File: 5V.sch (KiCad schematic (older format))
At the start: 13 parts, among them U2 LMZ13608, U3 LTC2946

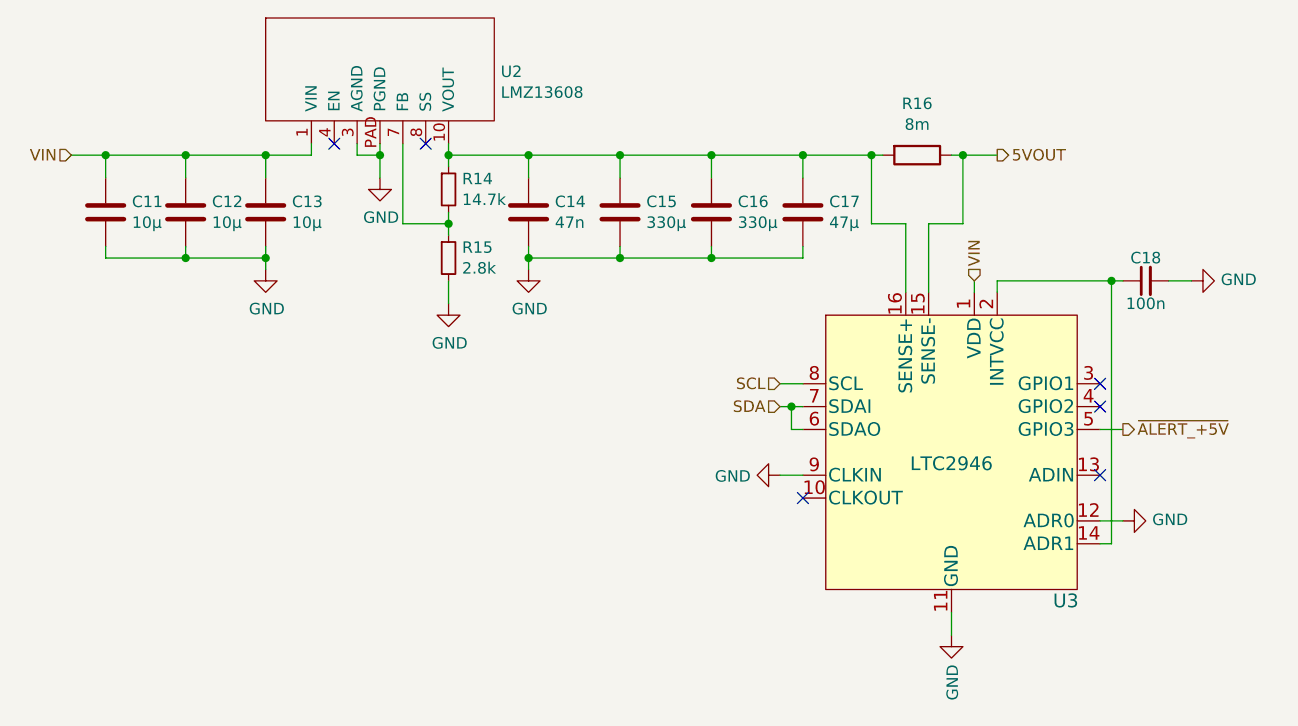
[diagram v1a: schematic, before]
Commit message: LMZM23600 from kicad libs
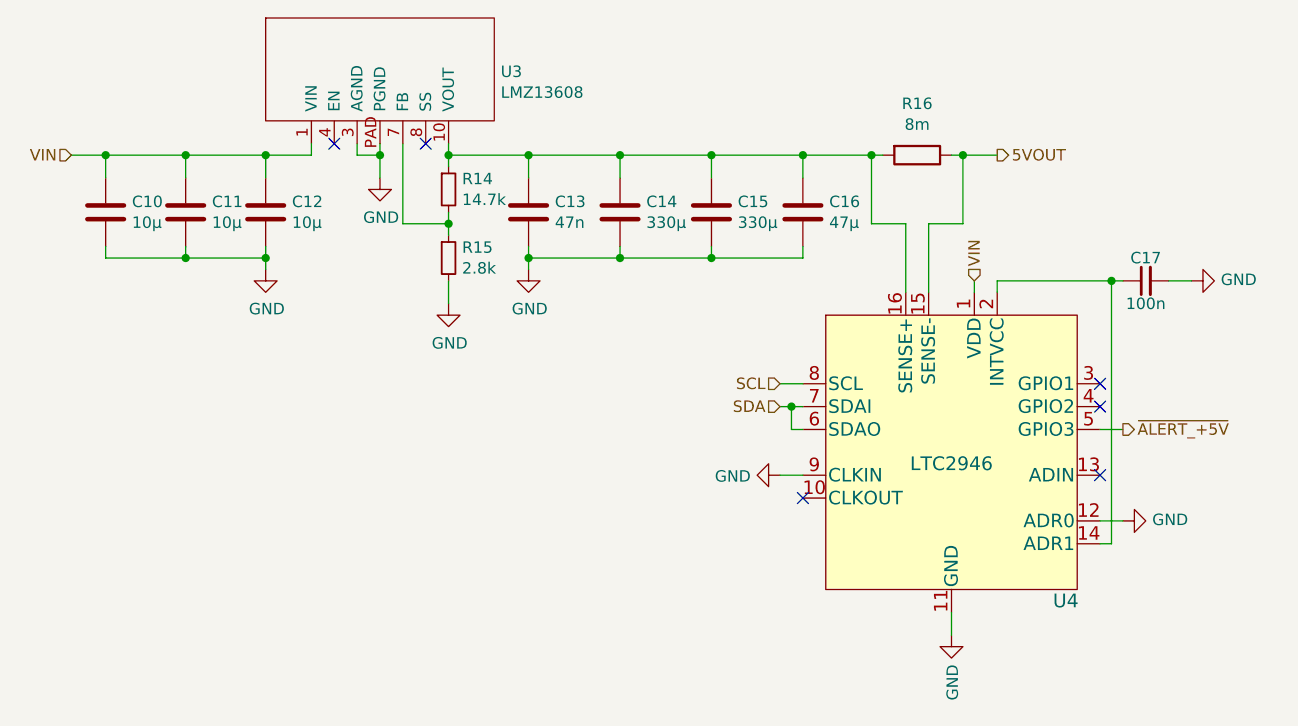
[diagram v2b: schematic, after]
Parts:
- renumbered C11 to C10, C12 to C11, C13 to C12, C14 to C13, C15 to C14, C16 to C15, C17 to C16, C18 to C17, U2 to U3, U3 to U4
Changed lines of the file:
@@
 $EndDescr
 $Comp
-L power:GND #PWR018
+L power:GND #PWR025
 U 1 1 5C2D1347
 P 6550 4350
-F 0 "#PWR018" H 6550 4100 50  0001 C CNN
+F 0 "#PWR025" H 6550 4100 50  0001 C CNN
 F 1 "GND" V 6555 4222 50  0000 R CNN
 F 2 "" H 6550 4350 50  0001 C CNN
@@
 $EndComp
 $Comp
-L Device:C_Small C18
+L Device:C_Small C17
 U 1 1 5C2D15AF
 P 6650 3300
-F 0 "C18" V 6750 3300 50  0000 C CNN
+F 0 "C17" V 6750 3300 50  0000 C CNN
 F 1 "100n" V 6550 3300 50  0000 C CNN
 F 2 "Capacitor_SMD:C_0603_1608Metric" H 6650 3300 50  0001 C CNN
@@
 $EndComp
 $Comp
-L power:GND #PWR019
+L power:GND #PWR026
 U 1 1 5C2D16C8
 P 6850 3300
-F 0 "#PWR019" H 6850 3050 50  0001 C CNN
+F 0 "#PWR026" H 6850 3050 50  0001 C CNN
 F 1 "GND" V 6855 3172 50  0000 R CNN
 F 2 "" H 6850 3300 50  0001 C CNN
@@
 $EndComp
 $Comp
-L LMZ13608:LMZ13608 U2
+L LMZ13608:LMZ13608 U3
 U 1 1 5C2D7DB3
 P 3300 2350
-F 0 "U2" H 3828 2315 50  0000 L CNN
+F 0 "U3" H 3828 2315 50  0000 L CNN
 F 1 "LMZ13608" H 3828 2224 50  0000 L CNN
 F 2 "LMZ13608:LMZ13608" H 3300 2350 50  0001 C CNN
@@
 Connection ~ 3300 2750
 $Comp
-L power:GND #PWR013
+L power:GND #PWR020
 U 1 1 5C2D92A7
 P 3300 2850
-F 0 "#PWR013" H 3300 2600 50  0001 C CNN
+F 0 "#PWR020" H 3300 2600 50  0001 C CNN
 F 1 "GND" H 3305 2677 50  0000 C CNN
 F 2 "" H 3300 2850 50  0001 C CNN
@@
 	3600 3300 3600 3400
 $Comp
-L power:GND #PWR014
+L power:GND #PWR021
 U 1 1 5C2DA3DE
 P 3600 3400
-F 0 "#PWR014" H 3600 3150 50  0001 C CNN
+F 0 "#PWR021" H 3600 3150 50  0001 C CNN
 F 1 "GND" H 3605 3227 50  0000 C CNN
 F 2 "" H 3600 3400 50  0001 C CNN
@@
 NoConn ~ 3500 2700
 $Comp
-L Device:C C14
+L Device:C C13
 U 1 1 5C2DC0D6
 P 3950 3000
-F 0 "C14" H 4065 3046 50  0000 L CNN
+F 0 "C13" H 4065 3046 50  0000 L CNN
 F 1 "47n" H 4065 2955 50  0000 L CNN
 F 2 "Capacitor_SMD:C_0603_1608Metric" H 3988 2850 50  0001 C CNN
@@
 	3950 3150 3950 3200
 $Comp
-L power:GND #PWR015
+L power:GND #PWR022
 U 1 1 5C2DD631
 P 3950 3250
-F 0 "#PWR015" H 3950 3000 50  0001 C CNN
+F 0 "#PWR022" H 3950 3000 50  0001 C CNN
 F 1 "GND" H 3955 3077 50  0000 C CNN
 F 2 "" H 3950 3250 50  0001 C CNN
@@
 $EndComp
 $Comp
-L Device:C C15
+L Device:C C14
 U 1 1 5C2DD6B4
 P 4350 3000
-F 0 "C15" H 4465 3046 50  0000 L CNN
+F 0 "C14" H 4465 3046 50  0000 L CNN
 F 1 "330µ" H 4465 2955 50  0000 L CNN
 F 2 "Capacitor_Tantalum_SMD:CP_EIA-7343-31_Kemet-D" H 4388 2850 50  0001 C CNN
@@
 $EndComp
 $Comp
-L Device:C C16
+L Device:C C15
 U 1 1 5C2DDE4E
 P 4750 3000
-F 0 "C16" H 4865 3046 50  0000 L CNN
+F 0 "C15" H 4865 3046 50  0000 L CNN
 F 1 "330µ" H 4865 2955 50  0000 L CNN
 F 2 "Capacitor_Tantalum_SMD:CP_EIA-7343-31_Kemet-D" H 4788 2850 50  0001 C CNN
@@
 $EndComp
 $Comp
-L Device:C C17
+L Device:C C16
 U 1 1 5C2DDE91
 P 5150 3000
-F 0 "C17" H 5265 3046 50  0000 L CNN
+F 0 "C16" H 5265 3046 50  0000 L CNN
 F 1 "47µ" H 5265 2955 50  0000 L CNN
 F 2 "Capacitor_SMD:C_1206_3216Metric" H 5188 2850 50  0001 C CNN
@@
 	4350 3200 4750 3200
 $Comp
-L Device:C C13
+L Device:C C12
 U 1 1 5C2E1567
 P 2800 3000
-F 0 "C13" H 2915 3046 50  0000 L CNN
+F 0 "C12" H 2915 3046 50  0000 L CNN
 F 1 "10µ" H 2915 2955 50  0000 L CNN
 F 2 "Capacitor_SMD:C_1210_3225Metric" H 2838 2850 50  0001 C CNN
@@
 	2800 2750 3000 2750
 $Comp
-L power:GND #PWR012
+L power:GND #PWR019
 U 1 1 5C2E20F7
 P 2800 3250
-F 0 "#PWR012" H 2800 3000 50  0001 C CNN
+F 0 "#PWR019" H 2800 3000 50  0001 C CNN
 F 1 "GND" H 2805 3077 50  0000 C CNN
 F 2 "" H 2800 3250 50  0001 C CNN
@@
 	5150 4150 5050 4150
 $Comp
-L power:GND #PWR016
+L power:GND #PWR023
 U 1 1 5C370C74
 P 5050 4150
-F 0 "#PWR016" H 5050 3900 50  0001 C CNN
+F 0 "#PWR023" H 5050 3900 50  0001 C CNN
 F 1 "GND" V 5055 4022 50  0000 R CNN
 F 2 "" H 5050 4150 50  0001 C CNN
@@
 $EndComp
 $Comp
-L power:GND #PWR017
+L power:GND #PWR024
 U 1 1 5C370DDF
 P 5800 4850
-F 0 "#PWR017" H 5800 4600 50  0001 C CNN
+F 0 "#PWR024" H 5800 4600 50  0001 C CNN
 F 1 "GND" V 5805 4722 50  0000 R CNN
 F 2 "" H 5800 4850 50  0001 C CNN
@@
 NoConn ~ 6450 4150
 $Comp
-L LTC2946:LTC2946 U3
+L LTC2946:LTC2946 U4
 U 1 1 5C32FA1C
 P 5800 4050
-F 0 "U3" H 6300 3400 60  0000 C CNN
+F 0 "U4" H 6300 3400 60  0000 C CNN
 F 1 "LTC2946" H 5800 4000 60  0000 C CNN
 F 2 "Package_SO:MSOP-16_3x4mm_P0.5mm" H 6250 3200 60  0001 C CNN
@@
 $EndComp
 $Comp
-L Device:C C12
+L Device:C C11
 U 1 1 5C709529
 P 2450 3000
-F 0 "C12" H 2565 3046 50  0000 L CNN
+F 0 "C11" H 2565 3046 50  0000 L CNN
 F 1 "10µ" H 2565 2955 50  0000 L CNN
 F 2 "Capacitor_SMD:C_1210_3225Metric" H 2488 2850 50  0001 C CNN
@@
 $EndComp
 $Comp
-L Device:C C11
+L Device:C C10
 U 1 1 5C709573
 P 2100 3000
-F 0 "C11" H 2215 3046 50  0000 L CNN
+F 0 "C10" H 2215 3046 50  0000 L CNN
 F 1 "10µ" H 2215 2955 50  0000 L CNN
 F 2 "Capacitor_SMD:C_1210_3225Metric" H 2138 2850 50  0001 C CNN

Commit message: more LEDs
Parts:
- renumbered R14 to R18, R15 to R19, R16 to R20
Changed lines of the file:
@@
 $EndComp
 $Comp
-L Device:R_Small R14
+L Device:R_Small R18
 U 1 1 5C2D93AE
 P 3600 2900
-F 0 "R14" H 3659 2946 50  0000 L CNN
+F 0 "R18" H 3659 2946 50  0000 L CNN
 F 1 "14.7k" H 3659 2855 50  0000 L CNN
 F 2 "Resistor_SMD:R_0603_1608Metric" H 3600 2900 50  0001 C CNN
@@
 $EndComp
 $Comp
-L Device:R_Small R15
+L Device:R_Small R19
 U 1 1 5C2D93E0
 P 3600 3200
-F 0 "R15" H 3659 3246 50  0000 L CNN
+F 0 "R19" H 3659 3246 50  0000 L CNN
 F 1 "2.8k" H 3659 3155 50  0000 L CNN
 F 2 "Resistor_SMD:R_0603_1608Metric" H 3600 3200 50  0001 C CNN
@@
 	2450 3200 2800 3200
 $Comp
-L Device:R R16
+L Device:R R20
 U 1 1 5C722741
 P 5650 2750
-F 0 "R16" V 5425 2750 50  0000 C CNN
+F 0 "R20" V 5425 2750 50  0000 C CNN
 F 1 "8m" V 5516 2750 50  0000 C CNN
 F 2 "Resistor_SMD:R_2010_5025Metric" V 5580 2750 50  0001 C CNN

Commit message: even more layout
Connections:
- net 5VOUT: now also C17.1, U4.1 (VDD), U4.14 (ADR1), U4.2 (INTVCC)
- net VIN: no longer U4.1 (VDD)
- net 5VIN: now reaches C13.1, C14.1, C15.1, C16.1, R18.1, R20.2, U3.10 (VOUT), U3.11 (VOUT), U4.16 (SENSE+)
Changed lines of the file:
@@
 $Descr A4 11693 8268
 encoding utf-8
-Sheet 4 6
+Sheet 6 6
 Title "ToolboxPlane PDB: 5V Regulator + Monitoring"
 Date "2019-01-03"
@@
 	1    0    0    -1
 $EndComp
-Text HLabel 5900 3300 1    50   Input ~ 0
-VIN
 Text HLabel 1950 2750 0    50   Input ~ 0
 VIN
@@
 Wire Wire Line
 	6750 3300 6850 3300
-Wire Wire Line
-	5900 3300 5900 3350
 Wire Wire Line
 	5050 3750 5150 3750
@@
 Connection ~ 5150 2750
 Wire Wire Line
-	5150 2750 5450 2750
+	5150 2750 5300 2750
 Wire Wire Line
 	5800 2750 5850 2750
@@
 Connection ~ 5850 2750
 Wire Wire Line
-	5850 2750 6000 2750
+	5850 2750 5950 2750
 Wire Wire Line
 	5450 2750 5450 3050
@@
 Wire Wire Line
 	5700 3050 5850 3050
+Text HLabel 5300 2650 1    50   Input ~ 0
+5VIN
+Wire Wire Line
+	5300 2650 5300 2750
+Connection ~ 5300 2750
+Wire Wire Line
+	5300 2750 5450 2750
+Wire Wire Line
+	5900 3350 5900 3300
+Wire Wire Line
+	5900 3300 5950 3300
+Connection ~ 6000 3300
+Wire Wire Line
+	5950 3300 5950 2750
+Connection ~ 5950 3300
+Wire Wire Line
+	5950 3300 6000 3300
+Connection ~ 5950 2750
+Wire Wire Line
+	5950 2750 6000 2750
 $EndSCHEMATC

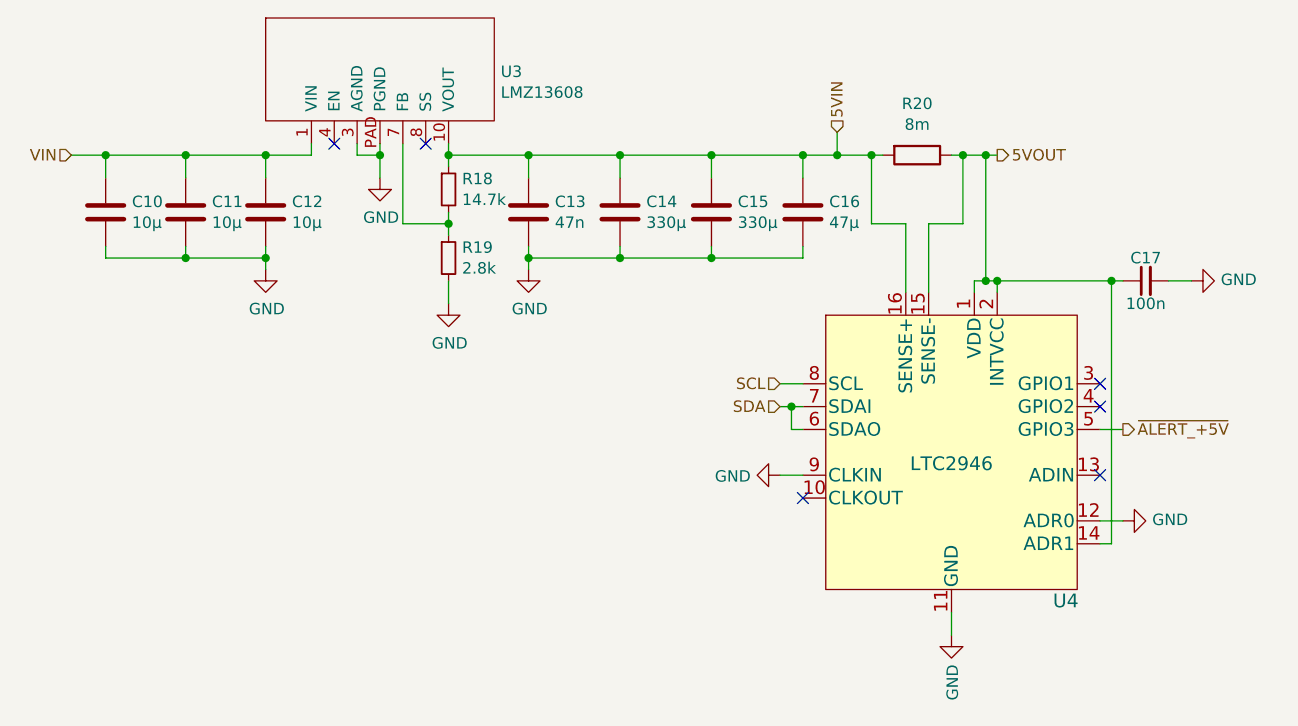
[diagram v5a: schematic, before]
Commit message: layout fixes, reannotate
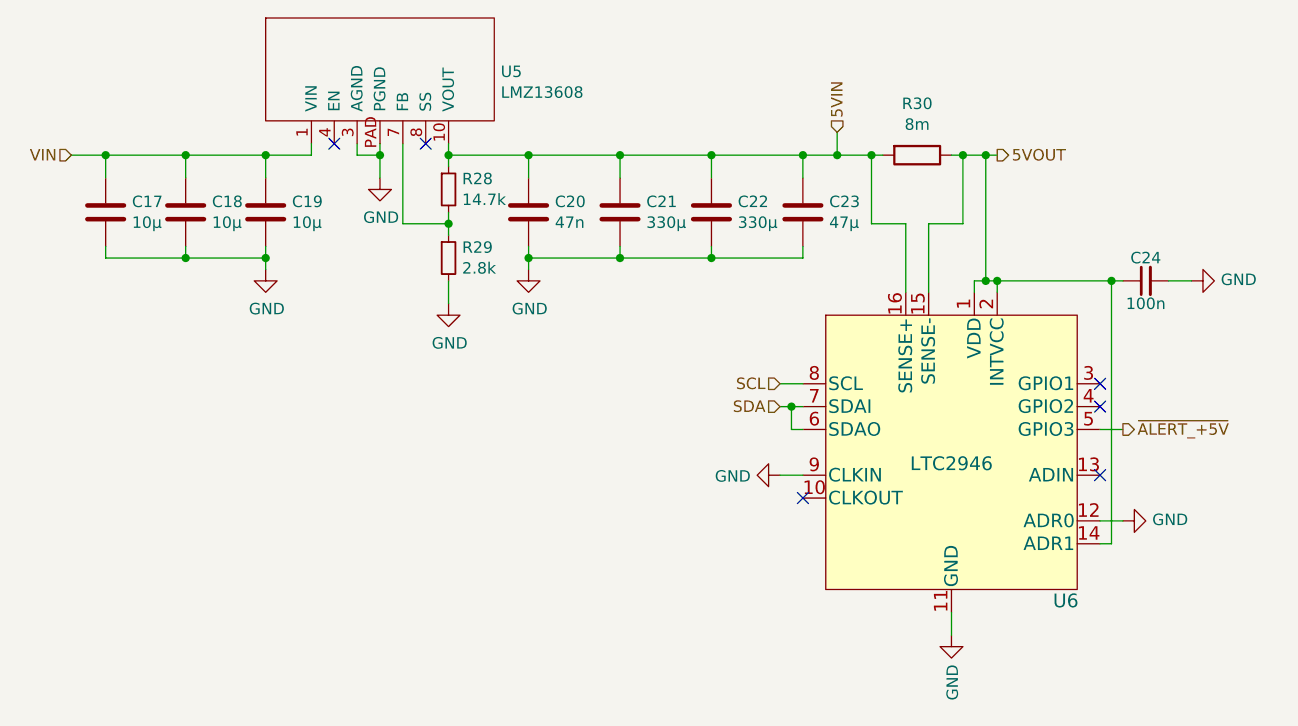
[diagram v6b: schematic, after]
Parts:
- renumbered C10 to C17, C11 to C18, C12 to C19, C13 to C20, C14 to C21, C15 to C22, C16 to C23, C17 to C24, R18 to R28, R19 to R29, R20 to R30, U3 to U5, U4 to U6
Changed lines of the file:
@@
 $EndDescr
 $Comp
-L power:GND #PWR034
+L power:GND #PWR058
 U 1 1 5C2D1347
 P 6550 4350
-F 0 "#PWR034" H 6550 4100 50  0001 C CNN
+F 0 "#PWR058" H 6550 4100 50  0001 C CNN
 F 1 "GND" V 6555 4222 50  0000 R CNN
 F 2 "" H 6550 4350 50  0001 C CNN
@@
 $EndComp
 $Comp
-L Device:C_Small C17
+L Device:C_Small C24
 U 1 1 5C2D15AF
 P 6650 3300
-F 0 "C17" V 6750 3300 50  0000 C CNN
+F 0 "C24" V 6750 3300 50  0000 C CNN
 F 1 "100n" V 6550 3300 50  0000 C CNN
 F 2 "Capacitor_SMD:C_0603_1608Metric" H 6650 3300 50  0001 C CNN
@@
 $EndComp
 $Comp
-L power:GND #PWR035
+L power:GND #PWR059
 U 1 1 5C2D16C8
 P 6850 3300
-F 0 "#PWR035" H 6850 3050 50  0001 C CNN
+F 0 "#PWR059" H 6850 3050 50  0001 C CNN
 F 1 "GND" V 6855 3172 50  0000 R CNN
 F 2 "" H 6850 3300 50  0001 C CNN
@@
 $EndComp
 $Comp
-L LMZ13608:LMZ13608 U3
+L LMZ13608:LMZ13608 U5
 U 1 1 5C2D7DB3
 P 3300 2350
-F 0 "U3" H 3828 2315 50  0000 L CNN
+F 0 "U5" H 3828 2315 50  0000 L CNN
 F 1 "LMZ13608" H 3828 2224 50  0000 L CNN
 F 2 "LMZ13608:LMZ13608" H 3300 2350 50  0001 C CNN
@@
 Connection ~ 3300 2750
 $Comp
-L power:GND #PWR029
+L power:GND #PWR053
 U 1 1 5C2D92A7
 P 3300 2850
-F 0 "#PWR029" H 3300 2600 50  0001 C CNN
+F 0 "#PWR053" H 3300 2600 50  0001 C CNN
 F 1 "GND" H 3305 2677 50  0000 C CNN
 F 2 "" H 3300 2850 50  0001 C CNN
@@
 $EndComp
 $Comp
-L Device:R_Small R18
+L Device:R_Small R28
 U 1 1 5C2D93AE
 P 3600 2900
-F 0 "R18" H 3659 2946 50  0000 L CNN
+F 0 "R28" H 3659 2946 50  0000 L CNN
 F 1 "14.7k" H 3659 2855 50  0000 L CNN
 F 2 "Resistor_SMD:R_0603_1608Metric" H 3600 2900 50  0001 C CNN
@@
 $EndComp
 $Comp
-L Device:R_Small R19
+L Device:R_Small R29
 U 1 1 5C2D93E0
 P 3600 3200
-F 0 "R19" H 3659 3246 50  0000 L CNN
+F 0 "R29" H 3659 3246 50  0000 L CNN
 F 1 "2.8k" H 3659 3155 50  0000 L CNN
 F 2 "Resistor_SMD:R_0603_1608Metric" H 3600 3200 50  0001 C CNN
@@
 	3600 3300 3600 3400
 $Comp
-L power:GND #PWR030
+L power:GND #PWR054
 U 1 1 5C2DA3DE
 P 3600 3400
-F 0 "#PWR030" H 3600 3150 50  0001 C CNN
+F 0 "#PWR054" H 3600 3150 50  0001 C CNN
 F 1 "GND" H 3605 3227 50  0000 C CNN
 F 2 "" H 3600 3400 50  0001 C CNN
@@
 NoConn ~ 3500 2700
 $Comp
-L Device:C C13
+L Device:C C20
 U 1 1 5C2DC0D6
 P 3950 3000
-F 0 "C13" H 4065 3046 50  0000 L CNN
+F 0 "C20" H 4065 3046 50  0000 L CNN
 F 1 "47n" H 4065 2955 50  0000 L CNN
 F 2 "Capacitor_SMD:C_0603_1608Metric" H 3988 2850 50  0001 C CNN
@@
 	3950 3150 3950 3200
 $Comp
-L power:GND #PWR031
+L power:GND #PWR055
 U 1 1 5C2DD631
 P 3950 3250
-F 0 "#PWR031" H 3950 3000 50  0001 C CNN
+F 0 "#PWR055" H 3950 3000 50  0001 C CNN
 F 1 "GND" H 3955 3077 50  0000 C CNN
 F 2 "" H 3950 3250 50  0001 C CNN
@@
 $EndComp
 $Comp
-L Device:C C14
+L Device:C C21
 U 1 1 5C2DD6B4
 P 4350 3000
-F 0 "C14" H 4465 3046 50  0000 L CNN
+F 0 "C21" H 4465 3046 50  0000 L CNN
 F 1 "330µ" H 4465 2955 50  0000 L CNN
 F 2 "Capacitor_Tantalum_SMD:CP_EIA-7343-31_Kemet-D" H 4388 2850 50  0001 C CNN
@@
 $EndComp
 $Comp
-L Device:C C15
+L Device:C C22
 U 1 1 5C2DDE4E
 P 4750 3000
-F 0 "C15" H 4865 3046 50  0000 L CNN
+F 0 "C22" H 4865 3046 50  0000 L CNN
 F 1 "330µ" H 4865 2955 50  0000 L CNN
 F 2 "Capacitor_Tantalum_SMD:CP_EIA-7343-31_Kemet-D" H 4788 2850 50  0001 C CNN
@@
 $EndComp
 $Comp
-L Device:C C16
+L Device:C C23
 U 1 1 5C2DDE91
 P 5150 3000
-F 0 "C16" H 5265 3046 50  0000 L CNN
+F 0 "C23" H 5265 3046 50  0000 L CNN
 F 1 "47µ" H 5265 2955 50  0000 L CNN
 F 2 "Capacitor_SMD:C_1206_3216Metric" H 5188 2850 50  0001 C CNN
@@
 	4350 3200 4750 3200
 $Comp
-L Device:C C12
+L Device:C C19
 U 1 1 5C2E1567
 P 2800 3000
-F 0 "C12" H 2915 3046 50  0000 L CNN
+F 0 "C19" H 2915 3046 50  0000 L CNN
 F 1 "10µ" H 2915 2955 50  0000 L CNN
 F 2 "Capacitor_SMD:C_1210_3225Metric" H 2838 2850 50  0001 C CNN
@@
 	2800 2750 3000 2750
 $Comp
-L power:GND #PWR028
+L power:GND #PWR052
 U 1 1 5C2E20F7
 P 2800 3250
-F 0 "#PWR028" H 2800 3000 50  0001 C CNN
+F 0 "#PWR052" H 2800 3000 50  0001 C CNN
 F 1 "GND" H 2805 3077 50  0000 C CNN
 F 2 "" H 2800 3250 50  0001 C CNN
@@
 	5150 4150 5050 4150
 $Comp
-L power:GND #PWR032
+L power:GND #PWR056
 U 1 1 5C370C74
 P 5050 4150
-F 0 "#PWR032" H 5050 3900 50  0001 C CNN
+F 0 "#PWR056" H 5050 3900 50  0001 C CNN
 F 1 "GND" V 5055 4022 50  0000 R CNN
 F 2 "" H 5050 4150 50  0001 C CNN
@@
 $EndComp
 $Comp
-L power:GND #PWR033
+L power:GND #PWR057
 U 1 1 5C370DDF
 P 5800 4850
-F 0 "#PWR033" H 5800 4600 50  0001 C CNN
+F 0 "#PWR057" H 5800 4600 50  0001 C CNN
 F 1 "GND" V 5805 4722 50  0000 R CNN
 F 2 "" H 5800 4850 50  0001 C CNN
@@
 NoConn ~ 6450 4150
 $Comp
-L LTC2946:LTC2946 U4
+L LTC2946:LTC2946 U6
 U 1 1 5C32FA1C
 P 5800 4050
-F 0 "U4" H 6300 3400 60  0000 C CNN
+F 0 "U6" H 6300 3400 60  0000 C CNN
 F 1 "LTC2946" H 5800 4000 60  0000 C CNN
 F 2 "Package_SO:MSOP-16_3x4mm_P0.5mm" H 6250 3200 60  0001 C CNN
@@
 $EndComp
 $Comp
-L Device:C C11
+L Device:C C18
 U 1 1 5C709529
 P 2450 3000
-F 0 "C11" H 2565 3046 50  0000 L CNN
+F 0 "C18" H 2565 3046 50  0000 L CNN
 F 1 "10µ" H 2565 2955 50  0000 L CNN
 F 2 "Capacitor_SMD:C_1210_3225Metric" H 2488 2850 50  0001 C CNN
@@
 $EndComp
 $Comp
-L Device:C C10
+L Device:C C17
 U 1 1 5C709573
 P 2100 3000
-F 0 "C10" H 2215 3046 50  0000 L CNN
+F 0 "C17" H 2215 3046 50  0000 L CNN
 F 1 "10µ" H 2215 2955 50  0000 L CNN
 F 2 "Capacitor_SMD:C_1210_3225Metric" H 2138 2850 50  0001 C CNN
@@
 	2450 3200 2800 3200
 $Comp
-L Device:R R20
+L Device:R R30
 U 1 1 5C722741
 P 5650 2750
-F 0 "R20" V 5425 2750 50  0000 C CNN
+F 0 "R30" V 5425 2750 50  0000 C CNN
 F 1 "8m" V 5516 2750 50  0000 C CNN
 F 2 "Resistor_SMD:R_2010_5025Metric" V 5580 2750 50  0001 C CNN
